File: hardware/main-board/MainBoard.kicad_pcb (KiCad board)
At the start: 4 copper layers, 145 parts, among them J1 Conn_01x03_Pin, J10 USB_C_Receptacle_USB2.0_14P, J11 Conn_02x05_Odd_Even, J12 Conn_01x02_Pin, J13 Conn_01x02_Pin, J2 Conn_01x03_Pin, J3 Conn_01x03_Pin, J4 Conn_01x03_Pin, J5 Conn_01x02_Pin, J6 Conn_01x02_Pin, J7 Conn_01x02_Pin, J8 Conn_01x02_Pin, J9 Barrel_Jack, SW1 SW_SP3T, SW2 SW_SP3T, SW3 SW_SPST, SW4 SW_SPST, U1 CD22M3494MQZ, U10 TL071, U11 CD22M3494MQZ, U12 CD22M3494MQZ, U13 TL071, U14 AD5263BRUZ200, U15 AD5263BRUZ200, U16 TL071, U17 CD22M3494MQZ, U18 CD22M3494MQZ, U19 TL071, U2 TL081, U20 AD5263BRUZ200, U21 AD5263BRUZ200, U22 TL071, U23 CD22M3494MQZ, U24 CD22M3494MQZ, U25 TL071, U26 AD5263BRUZ200, U27 AD5263BRUZ200, U28 TL071, U29 CD22M3494MQZ, U3 TL071, U30 CD22M3494MQZ, U31 XTPS55285VALR, U32 TPS54202DDC, U33 LM2776, U34 74HC164, U35 FT232RL, U36 74HC164, U37 STM32F091RCTx, U38 74HC164, U4 TL071, U5 TL071, U6 TL071, U7 TL071, U8 AD5263BRUZ200, U9 AD5263BRUZ200

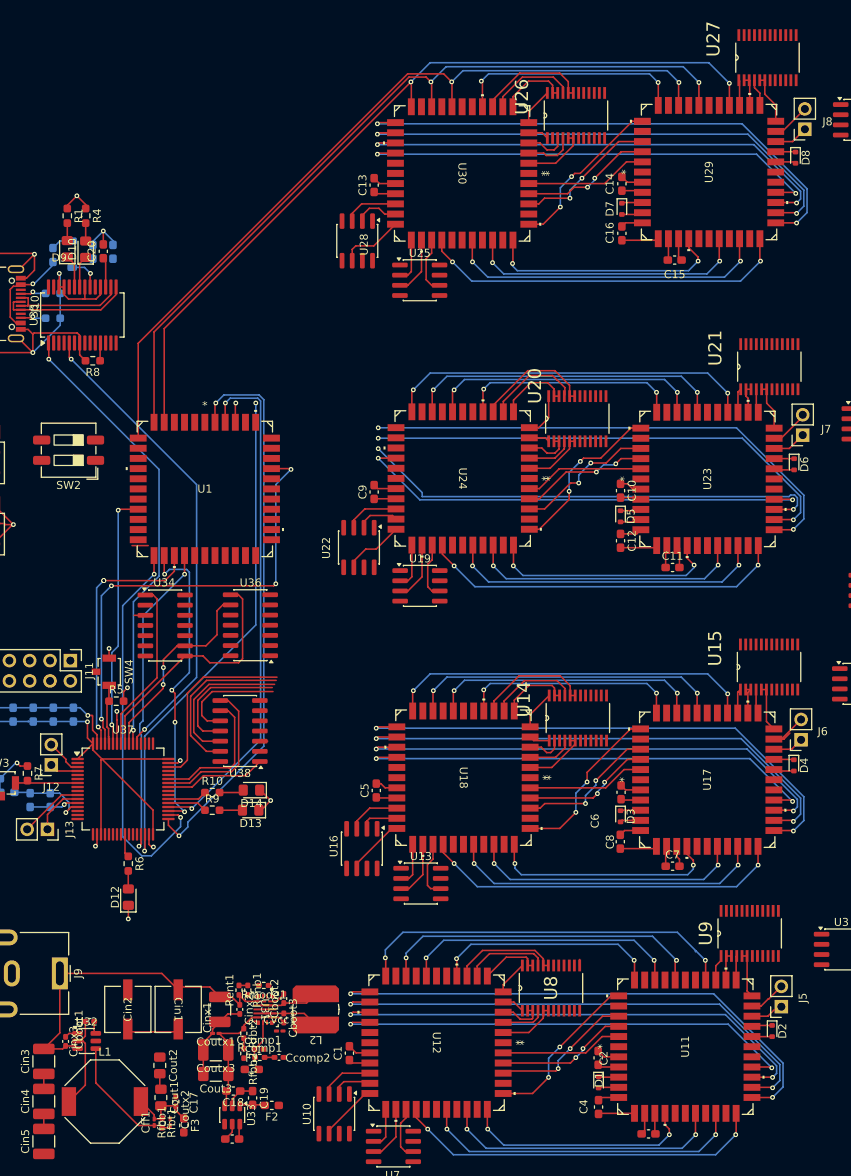
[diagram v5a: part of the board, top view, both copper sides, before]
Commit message: added some intercell connections
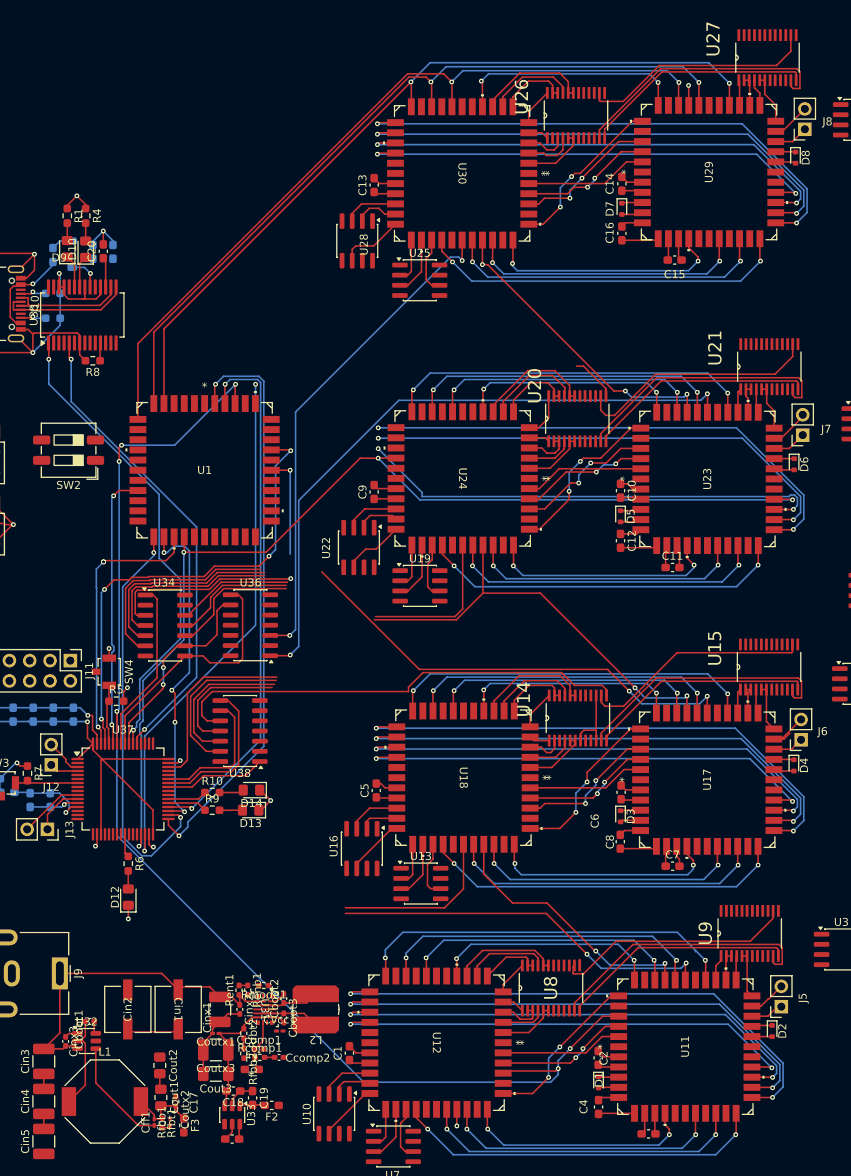
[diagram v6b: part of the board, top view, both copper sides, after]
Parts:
- moved U1 2.34 mm to (43.1, 80.6)
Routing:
- net /MicroController/MT_RST: track 77.9 -> 213.4 mm, vias 10 -> 12
- net /MicroController/SPI1_MOSI: track 0.00 -> 134.1 mm
- net /MicroController/MT_DAT: track 58.7 -> 188.9 mm, vias 4 -> 13
- net /MicroController/BRUZ_NRST: track 17.1 -> 135.8 mm
- net /MicroController/SPI1_SCK: track 0.00 -> 115.0 mm
- net /MicroController/MT_CS_7: track 0.00 -> 81.3 mm, vias 0 -> 2
- net /MicroController/MT_CS_1: track 0.00 -> 80.5 mm, vias 0 -> 2
- net /MicroController/MT_CS_3: track 0.00 -> 74.6 mm, vias 0 -> 2
- net /MicroController/MT_CS_8: track 0.00 -> 62.3 mm, vias 0 -> 2
- net /MicroController/BRUZ_NCS_4: track 13.7 -> 58.3 mm
- net /MicroController/MT_CS_2: track 0.00 -> 44.3 mm
- net /MicroController/MT_CS_4: track 0.00 -> 37.6 mm
- net /MicroController/MT_CS_0: track 4.25 -> 37.0 mm, vias 0 -> 2
- net /MicroController/MT_AY1: track 277.5 -> 309.0 mm
- net /MicroController/MT_CS_5: track 0.00 -> 15.5 mm
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
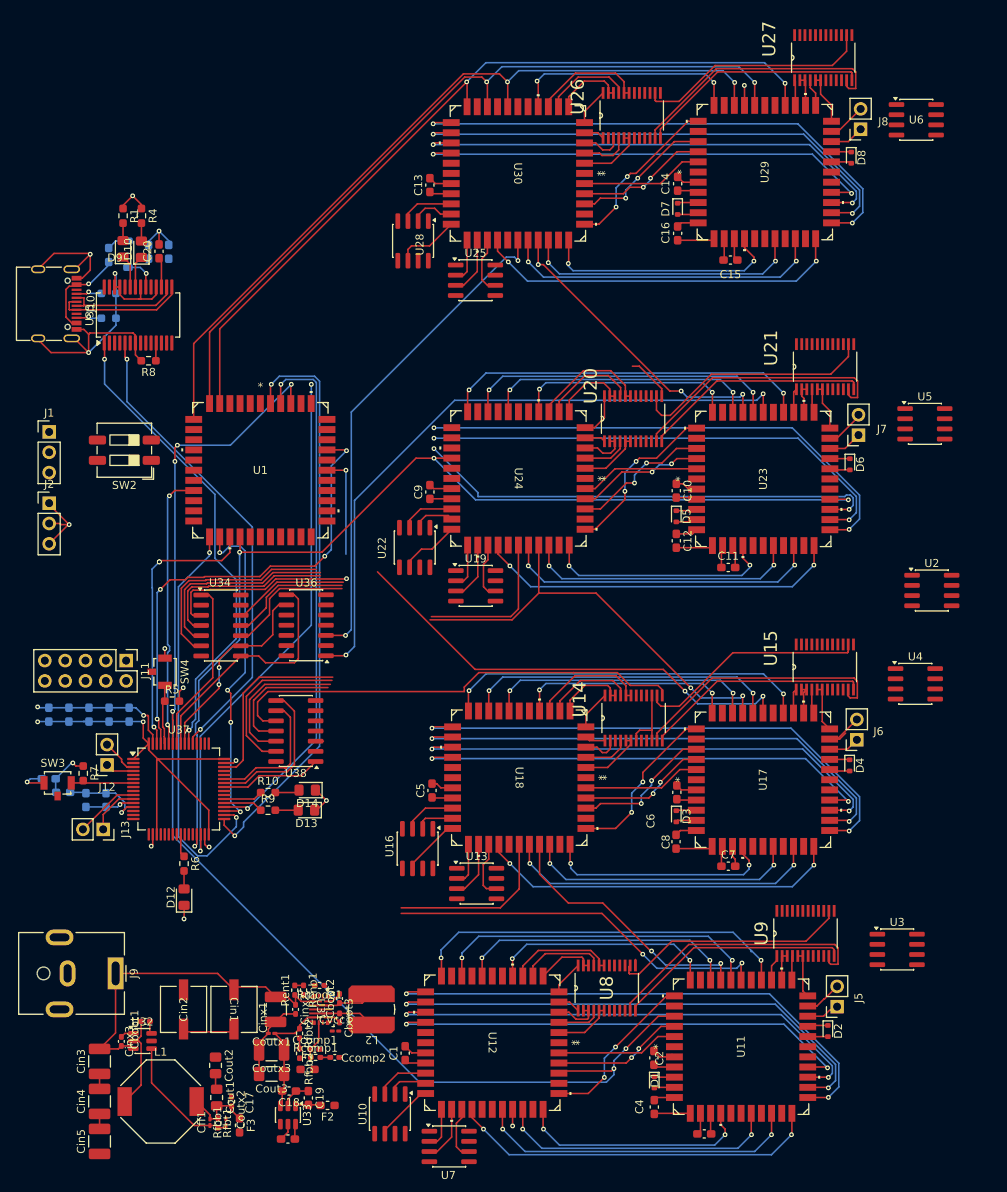
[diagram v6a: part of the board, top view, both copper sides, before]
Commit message: Squishing Standard Cells Together
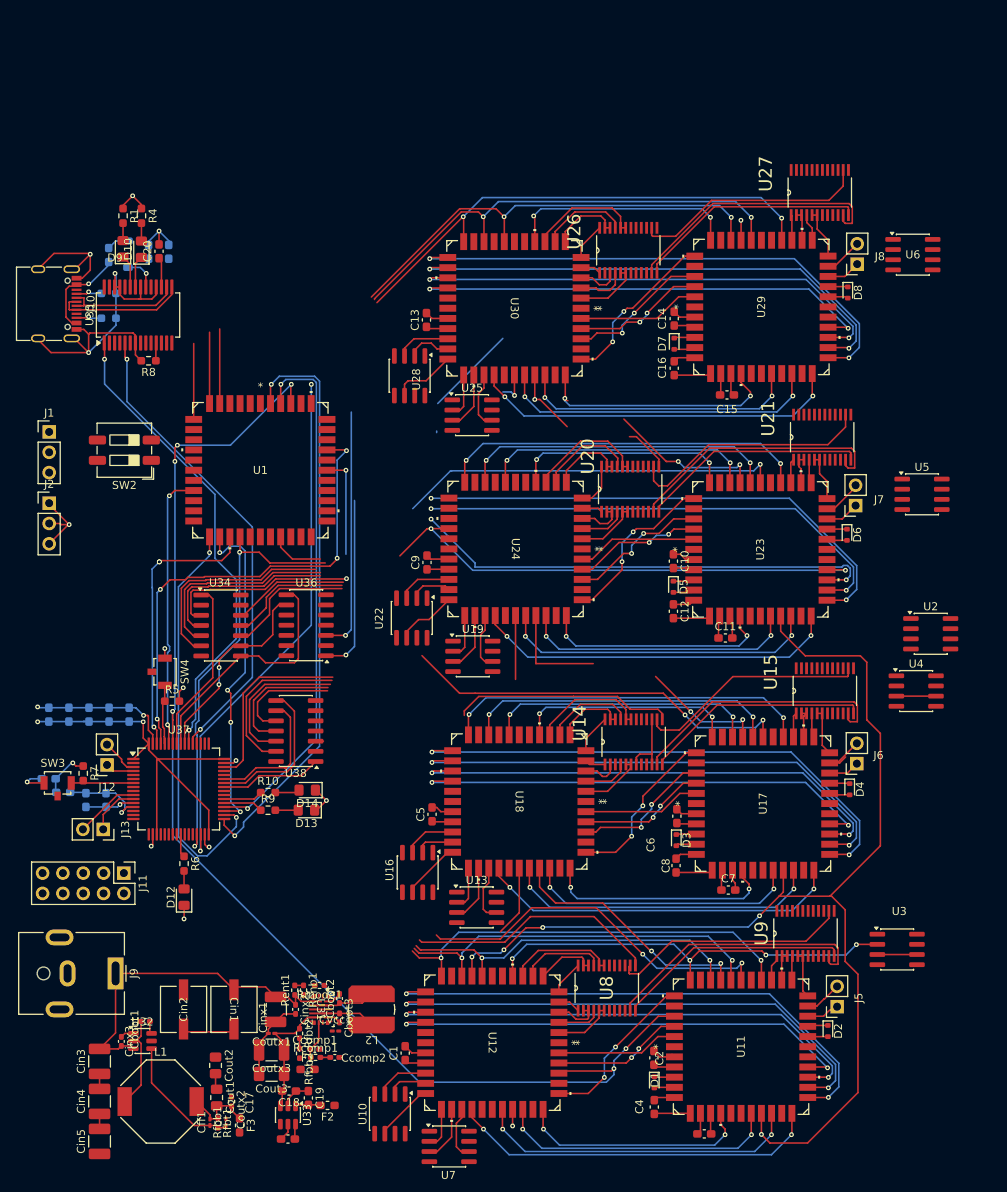
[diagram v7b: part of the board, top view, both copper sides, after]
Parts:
- moved J11 26.6 mm to (26.0, 131.0)
- moved C16 16.9 mm to (94.8, 67.9)
- moved D7 16.9 mm to (94.8, 64.8)
- moved C13 16.9 mm to (63.9, 61.8)
- moved C14 16.9 mm to (94.8, 61.7)
- moved D8 16.9 mm to (116.5, 58.4)
- moved J8 16.9 mm to (117.7, 54.8)
- moved U25 16.9 mm to (69.6, 73.7)
- moved U27 16.9 mm to (113.0, 45.9)
- moved U28 16.9 mm to (61.8, 68.8)
- moved U30 16.9 mm to (74.9, 60.4)
- moved U6 16.9 mm to (124.7, 53.7)
- moved C15 16.9 mm to (101.4, 71.2)
- moved U26 16.9 mm to (89.1, 53.1)
- moved U29 16.9 mm to (105.7, 60.2)
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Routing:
- net /MicroController/MT_STB: track 34.7 -> 179.2 mm, vias 2 -> 7
- net /MicroController/MT_DAT: track 188.9 -> 152.5 mm
- net /STD3/Y2: track 98.7 -> 66.7 mm
- net /MicroController/BRUZ_NCS_0: track 1.73 -> 33.3 mm
- net /STD3/Y1: track 98.1 -> 68.5 mm
- net /STD3/Y0: track 100.8 -> 72.3 mm
- net /Cell_0_Out: track 28.4 -> 53.1 mm, vias 2 -> 4
- net /MicroController/BRUZ_NCS_4: track 58.3 -> 41.3 mm
- net /MicroController/MT_CS_8: track 62.3 -> 46.7 mm
- net /MicroController/MT_AY1: track 309.0 -> 296.4 mm
- net /MicroController/MT_CS_4: track 37.6 -> 25.2 mm
- net /MicroController/MT_CS_2: track 44.3 -> 33.0 mm
- net /MicroController/MT_CS_7: track 81.3 -> 70.4 mm
- net /STD/Y2: track 35.2 -> 44.1 mm
- net /MicroController/MT_CS_1: track 80.5 -> 71.8 mm
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
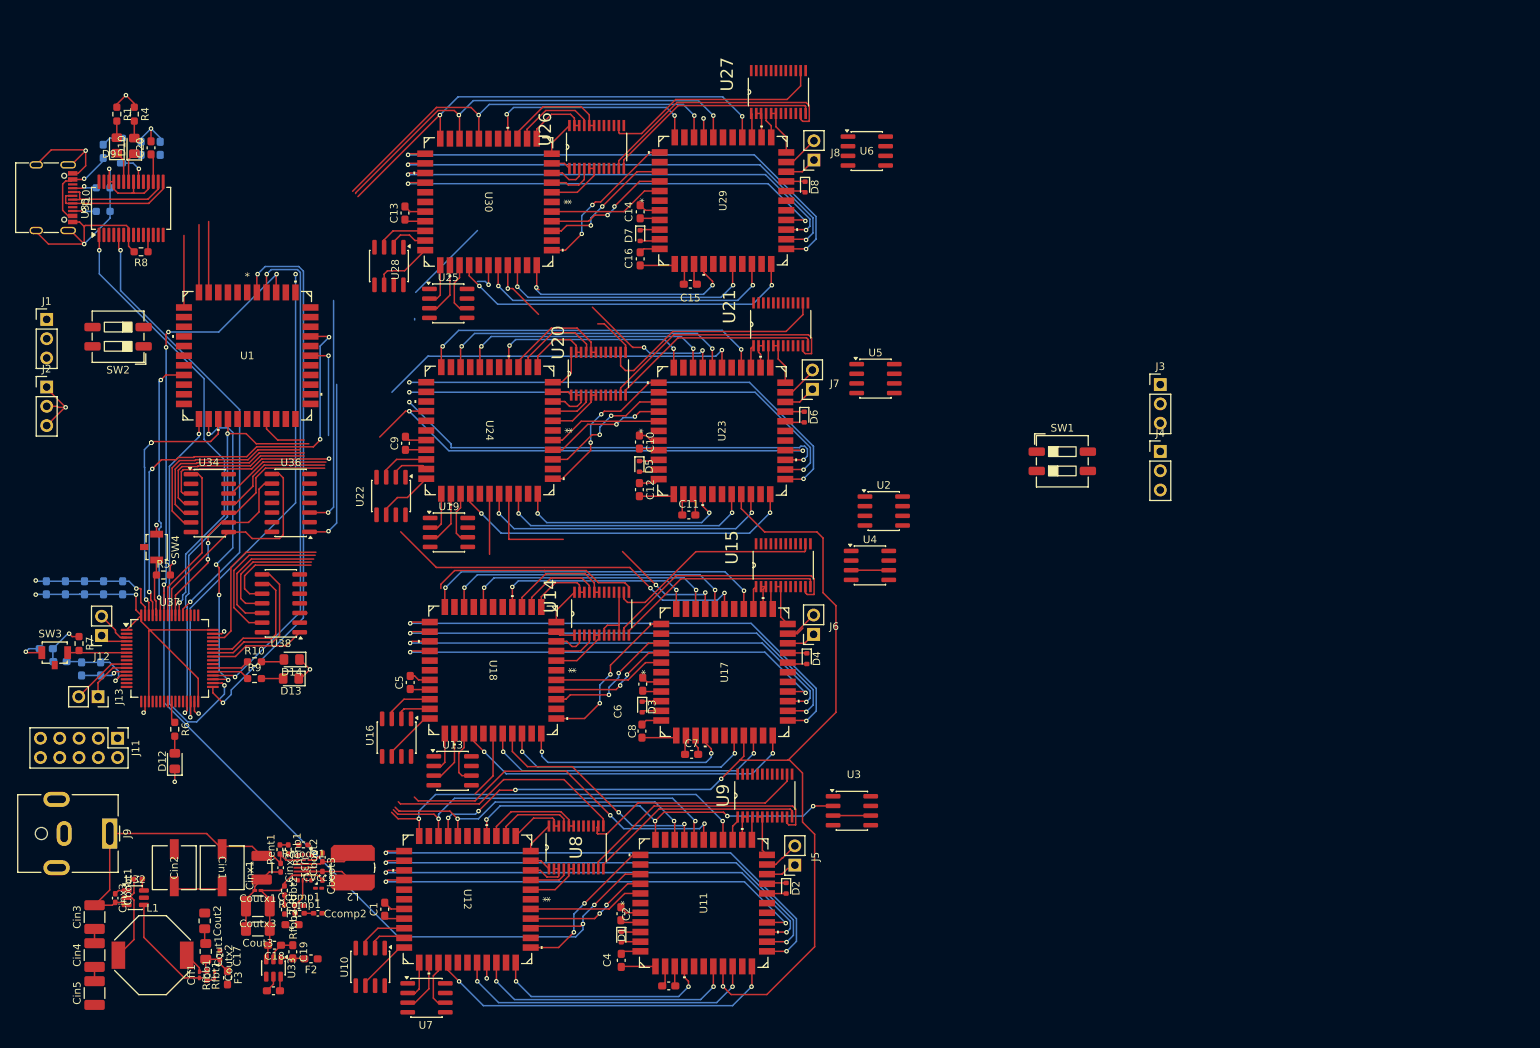
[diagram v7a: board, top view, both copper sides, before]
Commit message: started cross board traces for data and signal in bot cell
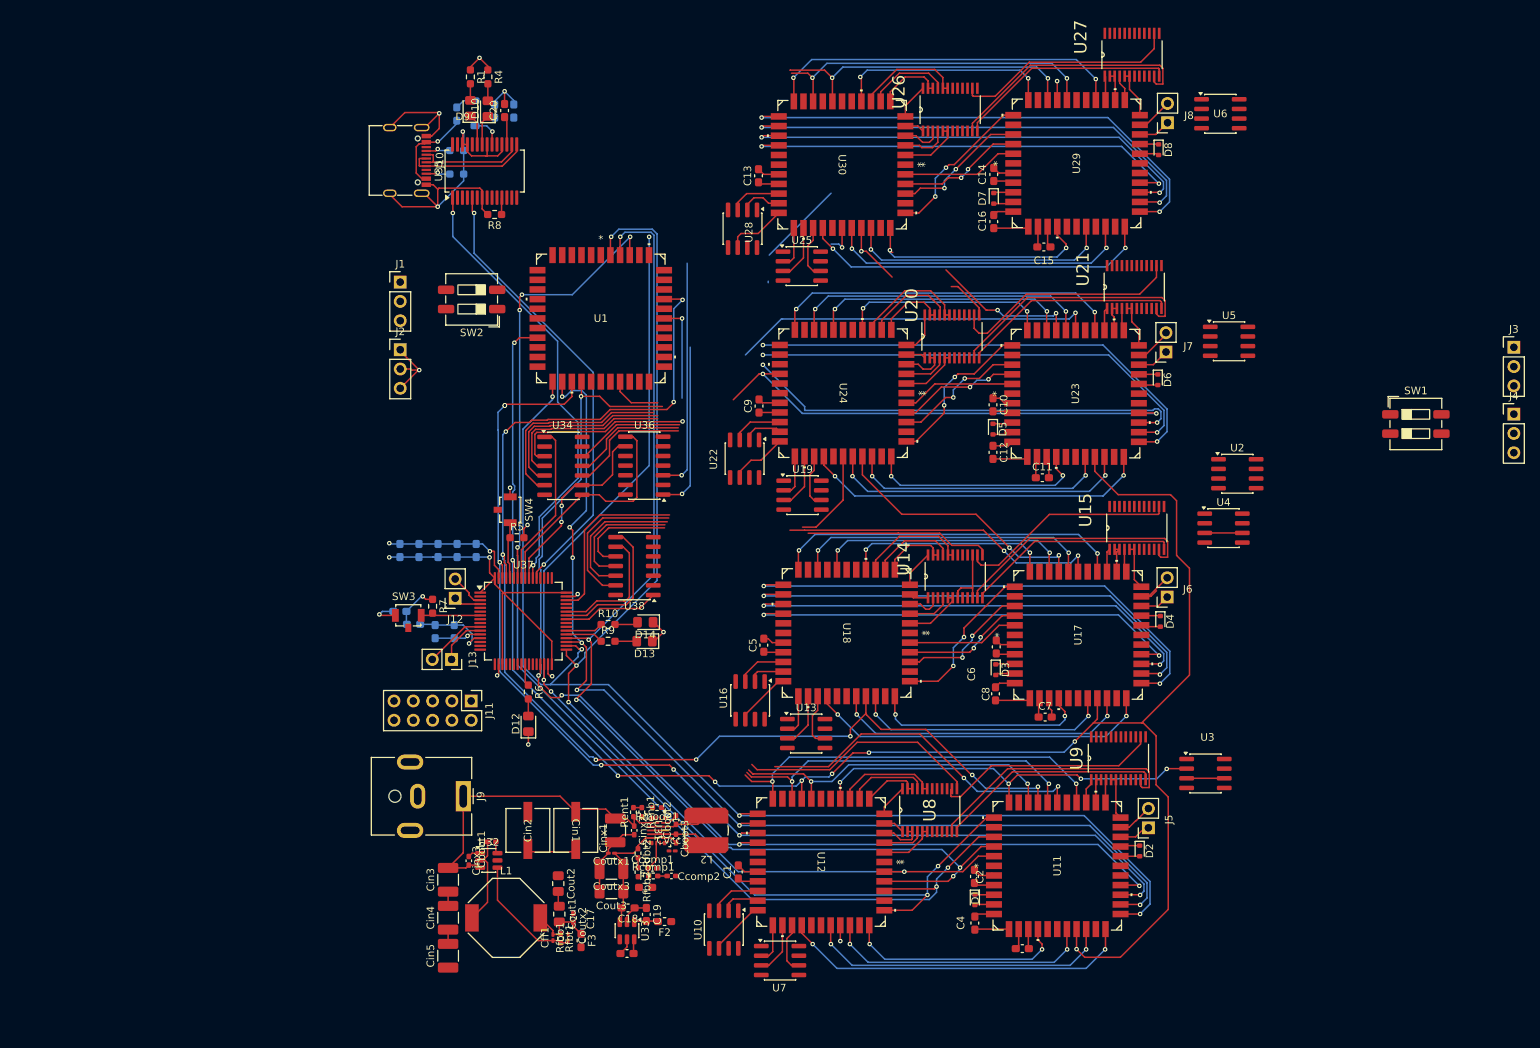
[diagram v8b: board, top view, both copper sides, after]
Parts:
- moved C14 46.8 mm to (141.4, 56.7)
- moved C16 46.8 mm to (141.4, 62.9)
- moved C4 46.8 mm to (138.9, 155.3)
- moved C8 46.8 mm to (141.6, 125.1)
- moved D7 46.8 mm to (141.4, 59.9)
- moved J7 46.8 mm to (164.0, 80.1)
- moved J8 46.8 mm to (164.3, 49.9)
- moved U2 46.8 mm to (173.4, 96.1)
- moved U23 46.8 mm to (152.1, 85.6)
- moved U29 46.8 mm to (152.3, 55.3)
- moved U30 46.8 mm to (121.4, 55.5)
- moved C13 46.8 mm to (110.4, 56.9)
- moved C26 46.8 mm to (70.7, 106.2)
- moved C29 46.8 mm to (70.3, 116.9)
- moved C9 46.8 mm to (110.5, 87.2)
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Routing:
- net /MicroController/MT_DAT: track 152.5 -> 229.8 mm, vias 13 -> 16
- net /MicroController/MT_AX3: track 132.4 -> 201.0 mm, vias 10 -> 11
- net /MicroController/MT_AY2: track 150.3 -> 212.8 mm, vias 10 -> 11
- net /MicroController/MT_STB: track 179.2 -> 238.4 mm, vias 7 -> 9
- net /MicroController/MT_AX0: track 133.5 -> 192.1 mm, vias 2 -> 4
- net /MicroController/MT_AY0: track 280.8 -> 335.7 mm, vias 11 -> 13
- net /MicroController/MT_AY1: track 296.4 -> 333.0 mm, vias 10 -> 11
- net /MicroController/MT_AX2: track 297.7 -> 333.5 mm, vias 12 -> 13
- net /MicroController/MT_AX1: track 317.1 -> 349.7 mm
- net /STD3/Y2: track 66.7 -> 41.6 mm
- net /STD3/Y0: track 72.3 -> 47.8 mm
- net /STD3/Y1: track 68.5 -> 44.1 mm
- net /MicroController/MT_CS_4: track 25.2 -> 16.3 mm
- net /MicroController/MT_CS_1: track 71.8 -> 65.2 mm
- net /MicroController/MT_CS_2: track 33.0 -> 37.6 mm
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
